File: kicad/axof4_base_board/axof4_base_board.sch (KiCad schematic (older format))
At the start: 1 part

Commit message: backup
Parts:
- added R21, R23: 4.7k, Resistor_SMD:R_1206_3216Metric_Pad1.42x1.75mm_HandSolder, symbol axof4_base_board-rescue:R-Device
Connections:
- wire segments 23 -> 34
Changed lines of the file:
@@
 $Descr A4 11693 8268
 encoding utf-8
-Sheet 1 4
+Sheet 1 5
 Title ""
 Date ""
@@
 $EndSheet
 $Comp
-L power:+3.3V #PWR03
+L axof4_base_board-rescue:+3.3V-power #PWR03
 U 1 1 5ECCC814
 P 6600 1000
@@
 $EndComp
 $Comp
-L power:+5V #PWR01
+L axof4_base_board-rescue:+5V-power #PWR01
 U 1 1 5ECCC81A
 P 6350 1000
@@
 Wire Wire Line
 	6350 1000 6350 1250
-$Comp
-L STM32F4DISCOVERY:STM32F4DISCOVERY JB1
-U 1 1 5ECCC823
-P 5550 4050
-AR Path="/5ECCC823" Ref="JB1"  Part="1"
-AR Path="/5EFDA4FE/5ECCC823" Ref="JB?"  Part="1"
-F 0 "JB1" H 5550 7117 50  0000 C CNN
-F 1 "STM32F4DISCOVERY" H 5550 7026 50  0000 C CNN
-F 2 "lib:MODULE_STM32F4DISCOVERY" H 5550 4050 50  0001 L BNN
-F 3 "6" H 5550 4050 50  0001 L BNN
-F 4 "STMicroelectronics" H 5550 4050 50  0001 L BNN "Field4"
-F 5 "Manufacturer Recommendations" H 5550 4050 50  0001 L BNN "Field5"
-	1    5550 4050
-	1    0    0    -1
-$EndComp
-Wire Wire Line
-	4000 4550 4750 4550
-Wire Wire Line
-	4750 4450 4000 4450
+Wire Wire Line
+	4000 4550 4050 4550
+Wire Wire Line
+	4750 4450 4050 4450
 Wire Wire Line
 	4550 4650 4750 4650
@@
 I2S_MCLK
 $Comp
-L power:GND #PWR?
+L axof4_base_board-rescue:GND-power #PWR?
 U 1 1 5ECCC838
 P 6350 6950
@@
 F1 "spiram.sch" 50
 $EndSheet
+$Sheet
+S 8900 2400 950  950
+U 5ED86ED4
+F0 "Power" 50
+F1 "power.sch" 50
+$EndSheet
+Wire Wire Line
+	6350 1450 6600 1450
+Wire Wire Line
+	6600 1000 6600 1450
+$Comp
+L STM32F4DISCOVERY:STM32F4DISCOVERY JB1
+U 1 1 5ECCC823
+P 5550 4050
+AR Path="/5ECCC823" Ref="JB1"  Part="1"
+AR Path="/5EFDA4FE/5ECCC823" Ref="JB?"  Part="1"
+F 0 "JB1" H 5550 7117 50  0000 C CNN
+F 1 "STM32F4DISCOVERY" H 5550 7026 50  0000 C CNN
+F 2 "lib:MODULE_STM32F4DISCOVERY" H 5550 4050 50  0001 L BNN
+F 3 "6" H 5550 4050 50  0001 L BNN
+F 4 "STMicroelectronics" H 5550 4050 50  0001 L BNN "Field4"
+F 5 "Manufacturer Recommendations" H 5550 4050 50  0001 L BNN "Field5"
+	1    5550 4050
+	1    0    0    -1
+$EndComp
+$Comp
+L axof4_base_board-rescue:R-Device R23
+U 1 1 5EDF8C2D
+P 3100 4200
+AR Path="/5EDF8C2D" Ref="R23"  Part="1"
+AR Path="/5EFC127A/5EDF8C2D" Ref="R?"  Part="1"
+F 0 "R23" H 3050 4100 50  0000 R CNN
+F 1 "4.7k" V 3100 4300 50  0000 R CNN
+F 2 "Resistor_SMD:R_1206_3216Metric_Pad1.42x1.75mm_HandSolder" V 3030 4200 50  0001 C CNN
+F 3 "~" H 3100 4200 50  0001 C CNN
+	1    3100 4200
+	-1   0    0    1
+$EndComp
+$Comp
+L axof4_base_board-rescue:+3.3V-power #PWR021
+U 1 1 5EDF8C33
+P 3100 4000
+AR Path="/5EDF8C33" Ref="#PWR021"  Part="1"
+AR Path="/5EFC127A/5EDF8C33" Ref="#PWR?"  Part="1"
+F 0 "#PWR021" H 3100 3850 50  0001 C CNN
+F 1 "+3.3V" H 3115 4173 50  0000 C CNN
+F 2 "" H 3100 4000 50  0001 C CNN
+F 3 "" H 3100 4000 50  0001 C CNN
+	1    3100 4000
+	1    0    0    -1
+$EndComp
+Wire Wire Line
+	3100 4000 3100 4050
+Connection ~ 3100 4050
+Wire Wire Line
+	2900 4050 3100 4050
+$Comp
+L axof4_base_board-rescue:R-Device R21
+U 1 1 5EDF8C3C
+P 2900 4200
+AR Path="/5EDF8C3C" Ref="R21"  Part="1"
+AR Path="/5EFC127A/5EDF8C3C" Ref="R?"  Part="1"
+F 0 "R21" H 3100 4100 50  0000 R CNN
+F 1 "4.7k" V 2900 4300 50  0000 R CNN
+F 2 "Resistor_SMD:R_1206_3216Metric_Pad1.42x1.75mm_HandSolder" V 2830 4200 50  0001 C CNN
+F 3 "~" H 2900 4200 50  0001 C CNN
+	1    2900 4200
+	-1   0    0    1
+$EndComp
+Wire Wire Line
+	3100 4350 4050 4350
+Wire Wire Line
+	4050 4350 4050 4450
+Connection ~ 4050 4450
+Wire Wire Line
+	4050 4450 4000 4450
+Wire Wire Line
+	2900 4350 2900 4650
+Wire Wire Line
+	2900 4650 4050 4650
+Wire Wire Line
+	4050 4650 4050 4550
+Connection ~ 4050 4550
+Wire Wire Line
+	4050 4550 4750 4550
 $EndSCHEMATC

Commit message: work on kicad project
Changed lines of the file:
@@
 $Descr A4 11693 8268
 encoding utf-8
-Sheet 1 5
+Sheet 1 6
 Title ""
 Date ""
@@
 Wire Wire Line
 	4050 4550 4750 4550
+$Sheet
+S 7750 3700 950  950
+U 5EE2DB57
+F0 "MIDI" 50
+F1 "midi.sch" 50
+$EndSheet
+Text GLabel 2900 1900 0    50   Input ~ 0
+MIDI_RX
+Text GLabel 2900 2050 0    50   Input ~ 0
+MIDI_TX
 $EndSCHEMATC

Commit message: cleanup, dedicated PCB WIP
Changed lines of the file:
@@
 $Descr A4 11693 8268
 encoding utf-8
-Sheet 1 6
+Sheet 1 7
 Title ""
 Date ""
@@
 Text GLabel 2900 2050 0    50   Input ~ 0
 MIDI_TX
+$Sheet
+S 8900 3700 950  950
+U 5F736ED6
+F0 "USB" 50
+F1 "usb.sch" 50
+$EndSheet
 $EndSCHEMATC

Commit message: kicad pcb backup, hohum axoctrl study
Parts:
- added J11: BOOT, symbol Connector:Conn_01x02_Male
- added J7: I2C1_HEADER, symbol Connector_Generic:Conn_02x04_Odd_Even
- added R36: 10k, symbol Device:R
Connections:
- net +3V3: now also J11.2 (Pin_2), J7.1 (Pin_1), J7.2 (Pin_2)
- net GND: now also J7.3 (Pin_3), J7.4 (Pin_4), R36.2
- net SPI2_SOFT_NSS: now reaches JB1.P1_22 (PB0)
- net I2C1_SDA: now reaches JB1.P2_20 (PB9)
- net I2C1_SDA: now also J7.7 (Pin_7), J7.8 (Pin_8)
- net at JB1.P2_21 (BOOT0): now also J11.1 (Pin_1), R36.1
- net I2C1_SCL: now reaches JB1.P2_23 (PB6)
- net I2C1_SCL: now also J7.5 (Pin_5), J7.6 (Pin_6)
- net I2C_SCL renamed WM8731_SCL
- net I2C_SDA renamed WM8731_SDA
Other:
- note added: "VCC\nGND"
- note removed: "TODO add header for external i2c devices"
- note removed: "TODO add header for external spi device"
- moved on the sheet: R21, R23
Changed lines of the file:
@@
 Wire Wire Line
 	4550 5750 4750 5750
-Text Notes 2000 4500 0    50   ~ 0
-TODO add header for external i2c devices
 Text GLabel 4000 4450 0    50   Input ~ 0
-I2C_SCL
+WM8731_SCL
 Text GLabel 4000 4550 0    50   Input ~ 0
-I2C_SDA
+WM8731_SDA
 Text GLabel 4550 4650 0    50   Input ~ 0
 I2S_LRCLK
@@
 Wire Wire Line
 	4500 3250 4750 3250
-Text Notes 2350 3250 0    50   ~ 0
-TODO add header for external spi device
 Text GLabel 4500 3750 0    50   Input ~ 0
 SPIRAM_SCK
@@
 L axof4_base_board-rescue:R-Device R23
 U 1 1 5EDF8C2D
-P 3100 4200
+P 3350 4150
 AR Path="/5EDF8C2D" Ref="R23"  Part="1"
 AR Path="/5EFC127A/5EDF8C2D" Ref="R?"  Part="1"
-F 0 "R23" H 3050 4100 50  0000 R CNN
-F 1 "4.7k" V 3100 4300 50  0000 R CNN
-F 2 "Resistor_SMD:R_1206_3216Metric_Pad1.42x1.75mm_HandSolder" V 3030 4200 50  0001 C CNN
-F 3 "~" H 3100 4200 50  0001 C CNN
-	1    3100 4200
+F 0 "R23" H 3300 4050 50  0000 R CNN
+F 1 "4.7k" V 3350 4250 50  0000 R CNN
+F 2 "Resistor_SMD:R_1206_3216Metric_Pad1.42x1.75mm_HandSolder" V 3280 4150 50  0001 C CNN
+F 3 "~" H 3350 4150 50  0001 C CNN
+	1    3350 4150
 	-1   0    0    1
 $EndComp
@@
 L axof4_base_board-rescue:+3.3V-power #PWR021
 U 1 1 5EDF8C33
-P 3100 4000
+P 3350 3950
 AR Path="/5EDF8C33" Ref="#PWR021"  Part="1"
 AR Path="/5EFC127A/5EDF8C33" Ref="#PWR?"  Part="1"
-F 0 "#PWR021" H 3100 3850 50  0001 C CNN
-F 1 "+3.3V" H 3115 4173 50  0000 C CNN
-F 2 "" H 3100 4000 50  0001 C CNN
-F 3 "" H 3100 4000 50  0001 C CNN
-	1    3100 4000
-	1    0    0    -1
-$EndComp
-Wire Wire Line
-	3100 4000 3100 4050
-Connection ~ 3100 4050
-Wire Wire Line
-	2900 4050 3100 4050
+F 0 "#PWR021" H 3350 3800 50  0001 C CNN
+F 1 "+3.3V" H 3365 4123 50  0000 C CNN
+F 2 "" H 3350 3950 50  0001 C CNN
+F 3 "" H 3350 3950 50  0001 C CNN
+	1    3350 3950
+	1    0    0    -1
+$EndComp
+Wire Wire Line
+	3350 3950 3350 4000
+Connection ~ 3350 4000
 $Comp
 L axof4_base_board-rescue:R-Device R21
 U 1 1 5EDF8C3C
-P 2900 4200
+P 3150 4150
 AR Path="/5EDF8C3C" Ref="R21"  Part="1"
 AR Path="/5EFC127A/5EDF8C3C" Ref="R?"  Part="1"
-F 0 "R21" H 3100 4100 50  0000 R CNN
-F 1 "4.7k" V 2900 4300 50  0000 R CNN
-F 2 "Resistor_SMD:R_1206_3216Metric_Pad1.42x1.75mm_HandSolder" V 2830 4200 50  0001 C CNN
-F 3 "~" H 2900 4200 50  0001 C CNN
-	1    2900 4200
+F 0 "R21" H 3350 4050 50  0000 R CNN
+F 1 "4.7k" V 3150 4250 50  0000 R CNN
+F 2 "Resistor_SMD:R_1206_3216Metric_Pad1.42x1.75mm_HandSolder" V 3080 4150 50  0001 C CNN
+F 3 "~" H 3150 4150 50  0001 C CNN
+	1    3150 4150
 	-1   0    0    1
 $EndComp
-Wire Wire Line
-	3100 4350 4050 4350
 Wire Wire Line
 	4050 4350 4050 4450
@@
 Wire Wire Line
 	4050 4450 4000 4450
-Wire Wire Line
-	2900 4350 2900 4650
-Wire Wire Line
-	2900 4650 4050 4650
 Wire Wire Line
 	4050 4650 4050 4550
@@
 F1 "midi.sch" 50
 $EndSheet
-Text GLabel 2900 1900 0    50   Input ~ 0
+Text GLabel 3150 1350 0    50   Input ~ 0
 MIDI_RX
-Text GLabel 2900 2050 0    50   Input ~ 0
+Text GLabel 3150 1500 0    50   Input ~ 0
 MIDI_TX
 $Sheet
@@
 F1 "usb.sch" 50
 $EndSheet
+$Comp
+L Connector_Generic:Conn_02x04_Odd_Even J7
+U 1 1 602901E8
+P 1300 4250
+F 0 "J7" H 1350 4567 50  0000 C CNN
+F 1 "I2C1_HEADER" H 1350 4476 50  0000 C CNN
+F 2 "" H 1300 4250 50  0001 C CNN
+F 3 "~" H 1300 4250 50  0001 C CNN
+	1    1300 4250
+	1    0    0    -1
+$EndComp
+Wire Wire Line
+	1600 4150 1100 4150
+Connection ~ 1600 4150
+$Comp
+L power:GND #PWR040
+U 1 1 602A0F05
+P 900 4300
+F 0 "#PWR040" H 900 4050 50  0001 C CNN
+F 1 "GND" H 905 4127 50  0000 C CNN
+F 2 "" H 900 4300 50  0001 C CNN
+F 3 "" H 900 4300 50  0001 C CNN
+	1    900  4300
+	1    0    0    -1
+$EndComp
+Wire Wire Line
+	900  4300 900  4250
+Wire Wire Line
+	900  4250 1100 4250
+Wire Wire Line
+	1100 4450 1600 4450
+Wire Wire Line
+	3150 4300 3150 4650
+Wire Wire Line
+	3350 4350 3350 4300
+Wire Wire Line
+	1600 4350 1100 4350
+Wire Wire Line
+	1600 3850 1600 4150
+Wire Wire Line
+	1100 4250 1600 4250
+Connection ~ 1100 4250
+Text Notes 1650 4250 0    50   ~ 0
+VCC\nGND
+$Comp
+L Connector:Conn_01x02_Male J11
+U 1 1 602C273A
+P 3900 1450
+F 0 "J11" H 3873 1332 50  0000 R CNN
+F 1 "BOOT" H 3873 1423 50  0000 R CNN
+F 2 "" H 3900 1450 50  0001 C CNN
+F 3 "~" H 3900 1450 50  0001 C CNN
+	1    3900 1450
+	1    0    0    1
+$EndComp
+Wire Wire Line
+	4100 1450 4150 1450
+Wire Wire Line
+	4700 1450 4700 1650
+Wire Wire Line
+	4700 1650 4750 1650
+$Comp
+L axof4_base_board-rescue:+3.3V-power #PWR048
+U 1 1 602C979F
+P 4150 1300
+AR Path="/602C979F" Ref="#PWR048"  Part="1"
+AR Path="/5EFC127A/602C979F" Ref="#PWR?"  Part="1"
+F 0 "#PWR048" H 4150 1150 50  0001 C CNN
+F 1 "+3.3V" H 4165 1473 50  0000 C CNN
+F 2 "" H 4150 1300 50  0001 C CNN
+F 3 "" H 4150 1300 50  0001 C CNN
+	1    4150 1300
+	1    0    0    -1
+$EndComp
+Wire Wire Line
+	4150 1300 4150 1350
+Wire Wire Line
+	4150 1350 4100 1350
+$Comp
+L Device:R R36
+U 1 1 602CD2A4
+P 4150 1600
+F 0 "R36" H 4220 1646 50  0000 L CNN
+F 1 "10k" H 4220 1555 50  0000 L CNN
+F 2 "" V 4080 1600 50  0001 C CNN
+F 3 "~" H 4150 1600 50  0001 C CNN
+	1    4150 1600
+	1    0    0    -1
+$EndComp
+Connection ~ 4150 1450
+Wire Wire Line
+	4150 1450 4700 1450
+$Comp
+L power:GND #PWR047
+U 1 1 602CE2E4
+P 4050 1800
+F 0 "#PWR047" H 4050 1550 50  0001 C CNN
+F 1 "GND" H 4055 1627 50  0000 C CNN
+F 2 "" H 4050 1800 50  0001 C CNN
+F 3 "" H 4050 1800 50  0001 C CNN
+	1    4050 1800
+	1    0    0    -1
+$EndComp
+Wire Wire Line
+	4050 1800 4050 1750
+Wire Wire Line
+	4050 1750 4150 1750
+Text GLabel 1600 4350 2    50   Input ~ 0
+I2C1_SCL
+Text GLabel 1600 4450 2    50   Input ~ 0
+I2C1_SDA
+Wire Wire Line
+	3150 4000 3350 4000
+Wire Wire Line
+	3350 4350 4050 4350
+Wire Wire Line
+	3150 4650 4050 4650
+Text GLabel 4500 4050 0    50   Input ~ 0
+I2C1_SCL
+Text GLabel 4500 4350 0    50   Input ~ 0
+I2C1_SDA
+Wire Wire Line
+	4500 4350 4750 4350
+Wire Wire Line
+	4500 4050 4750 4050
+Text GLabel 4500 3450 0    50   Input ~ 0
+SPI2_SOFT_NSS
+Wire Wire Line
+	4500 3450 4750 3450
+$Comp
+L axof4_base_board-rescue:+3.3V-power #PWR041
+U 1 1 603DAAD6
+P 1600 3850
+AR Path="/603DAAD6" Ref="#PWR041"  Part="1"
+AR Path="/5EFC127A/603DAAD6" Ref="#PWR?"  Part="1"
+F 0 "#PWR041" H 1600 3700 50  0001 C CNN
+F 1 "+3.3V" H 1615 4023 50  0000 C CNN
+F 2 "" H 1600 3850 50  0001 C CNN
+F 3 "" H 1600 3850 50  0001 C CNN
+	1    1600 3850
+	1    0    0    -1
+$EndComp
 $EndSCHEMATC

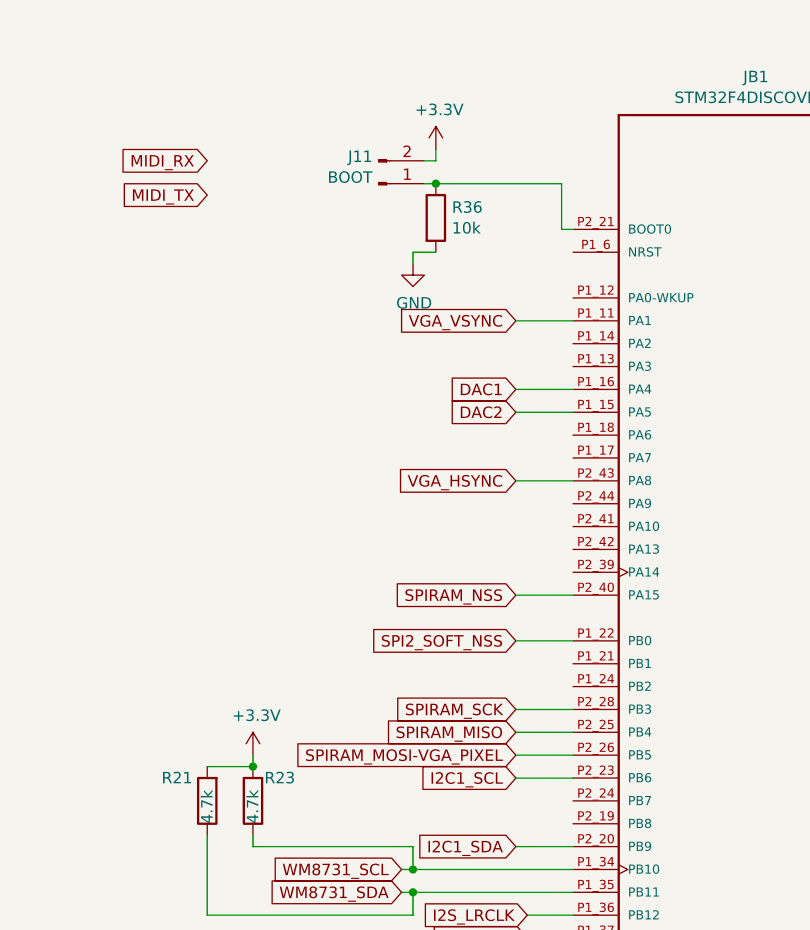
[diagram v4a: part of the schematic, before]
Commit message: rollback kicad project to use STM32F4DISCOVERY
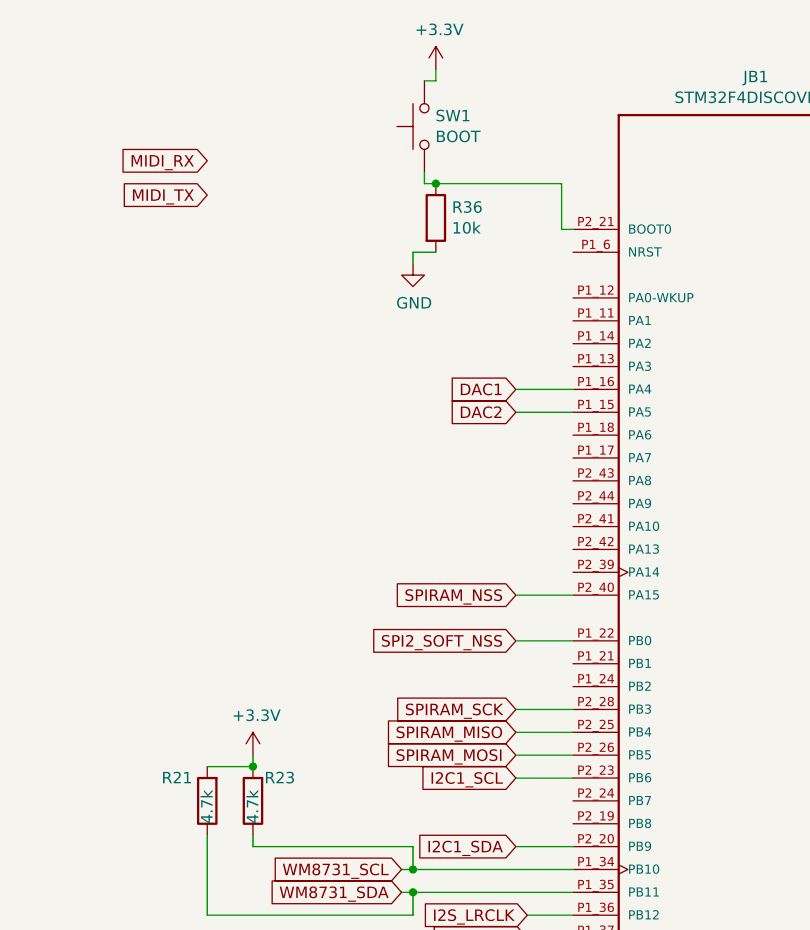
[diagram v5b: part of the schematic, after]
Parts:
- removed J11: BOOT, symbol Connector:Conn_01x02_Male
- added SW1: BOOT, Button_Switch_SMD:SW_Push_1P1T_NO_6x6mm_H9.5mm, symbol Switch:SW_Push
- J7: footprint (none) -> Connector_PinHeader_2.54mm:PinHeader_2x04_P2.54mm_Vertical
- R21, R23: footprint Resistor_SMD:R_1206_3216Metric_Pad1.42x1.75mm_HandSolder -> Resistor_SMD:R_0603_1608Metric
- R36: footprint (none) -> Resistor_SMD:R_0603_1608Metric
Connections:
- net +3V3: now also SW1.2
- net at JB1.P2_21 (BOOT0), R36.1: now also SW1.1
- net SPIRAM_MOSI-VGA_PIXEL renamed SPIRAM_MOSI
- net VGA_HSYNC: no longer names the net of JB1.P2_43 (PA8)
- net VGA_VSYNC: no longer names the net of JB1.P1_11 (PA1)
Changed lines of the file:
@@
 SPIRAM_MISO
 Text GLabel 4500 3950 0    50   Input ~ 0
-SPIRAM_MOSI-VGA_PIXEL
+SPIRAM_MOSI
 Wire Wire Line
 	4500 3750 4750 3750
@@
 Wire Wire Line
 	4500 3950 4750 3950
-Text GLabel 4500 2050 0    50   Input ~ 0
-VGA_VSYNC
-Wire Wire Line
-	4500 2050 4750 2050
-Text GLabel 4500 2750 0    50   Input ~ 0
-VGA_HSYNC
-Wire Wire Line
-	4500 2750 4750 2750
 $Sheet
 S 8900 1150 1000 900
@@
 F 0 "R23" H 3300 4050 50  0000 R CNN
 F 1 "4.7k" V 3350 4250 50  0000 R CNN
-F 2 "Resistor_SMD:R_1206_3216Metric_Pad1.42x1.75mm_HandSolder" V 3280 4150 50  0001 C CNN
+F 2 "Resistor_SMD:R_0603_1608Metric" V 3280 4150 50  0001 C CNN
 F 3 "~" H 3350 4150 50  0001 C CNN
 	1    3350 4150
@@
 F 0 "R21" H 3350 4050 50  0000 R CNN
 F 1 "4.7k" V 3150 4250 50  0000 R CNN
-F 2 "Resistor_SMD:R_1206_3216Metric_Pad1.42x1.75mm_HandSolder" V 3080 4150 50  0001 C CNN
+F 2 "Resistor_SMD:R_0603_1608Metric" V 3080 4150 50  0001 C CNN
 F 3 "~" H 3150 4150 50  0001 C CNN
 	1    3150 4150
@@
 F 0 "J7" H 1350 4567 50  0000 C CNN
 F 1 "I2C1_HEADER" H 1350 4476 50  0000 C CNN
-F 2 "" H 1300 4250 50  0001 C CNN
+F 2 "Connector_PinHeader_2.54mm:PinHeader_2x04_P2.54mm_Vertical" H 1300 4250 50  0001 C CNN
 F 3 "~" H 1300 4250 50  0001 C CNN
 	1    1300 4250
@@
 Text Notes 1650 4250 0    50   ~ 0
 VCC\nGND
-$Comp
-L Connector:Conn_01x02_Male J11
-U 1 1 602C273A
-P 3900 1450
-F 0 "J11" H 3873 1332 50  0000 R CNN
-F 1 "BOOT" H 3873 1423 50  0000 R CNN
-F 2 "" H 3900 1450 50  0001 C CNN
-F 3 "~" H 3900 1450 50  0001 C CNN
-	1    3900 1450
-	1    0    0    1
-$EndComp
 Wire Wire Line
 	4100 1450 4150 1450
@@
 L axof4_base_board-rescue:+3.3V-power #PWR048
 U 1 1 602C979F
-P 4150 1300
+P 4150 950
 AR Path="/602C979F" Ref="#PWR048"  Part="1"
 AR Path="/5EFC127A/602C979F" Ref="#PWR?"  Part="1"
-F 0 "#PWR048" H 4150 1150 50  0001 C CNN
-F 1 "+3.3V" H 4165 1473 50  0000 C CNN
-F 2 "" H 4150 1300 50  0001 C CNN
-F 3 "" H 4150 1300 50  0001 C CNN
-	1    4150 1300
-	1    0    0    -1
-$EndComp
-Wire Wire Line
-	4150 1300 4150 1350
-Wire Wire Line
-	4150 1350 4100 1350
+F 0 "#PWR048" H 4150 800 50  0001 C CNN
+F 1 "+3.3V" H 4165 1123 50  0000 C CNN
+F 2 "" H 4150 950 50  0001 C CNN
+F 3 "" H 4150 950 50  0001 C CNN
+	1    4150 950
+	1    0    0    -1
+$EndComp
+Wire Wire Line
+	4150 950  4150 1000
+Wire Wire Line
+	4150 1000 4100 1000
 $Comp
 L Device:R R36
@@
 F 0 "R36" H 4220 1646 50  0000 L CNN
 F 1 "10k" H 4220 1555 50  0000 L CNN
-F 2 "" V 4080 1600 50  0001 C CNN
+F 2 "Resistor_SMD:R_0603_1608Metric" V 4080 1600 50  0001 C CNN
 F 3 "~" H 4150 1600 50  0001 C CNN
 	1    4150 1600
@@
 	1    0    0    -1
 $EndComp
+$Comp
+L Switch:SW_Push SW1
+U 1 1 6102CCB9
+P 4100 1200
+F 0 "SW1" V 4146 1152 50  0000 R CNN
+F 1 "BOOT" V 4055 1152 50  0000 R CNN
+F 2 "Button_Switch_SMD:SW_Push_1P1T_NO_6x6mm_H9.5mm" H 4100 1400 50  0001 C CNN
+F 3 "~" H 4100 1400 50  0001 C CNN
+	1    4100 1200
+	0    -1   -1   0
+$EndComp
+Wire Wire Line
+	4100 1450 4100 1400
 $EndSCHEMATC
